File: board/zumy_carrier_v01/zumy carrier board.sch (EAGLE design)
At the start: 22 parts, among them IC1 SN74AUP2G17, IC2 SN74AUP2G17, J1 ODROID_POWER, J2 BATT_POWER, SW1 500SSP1S1M6QEA

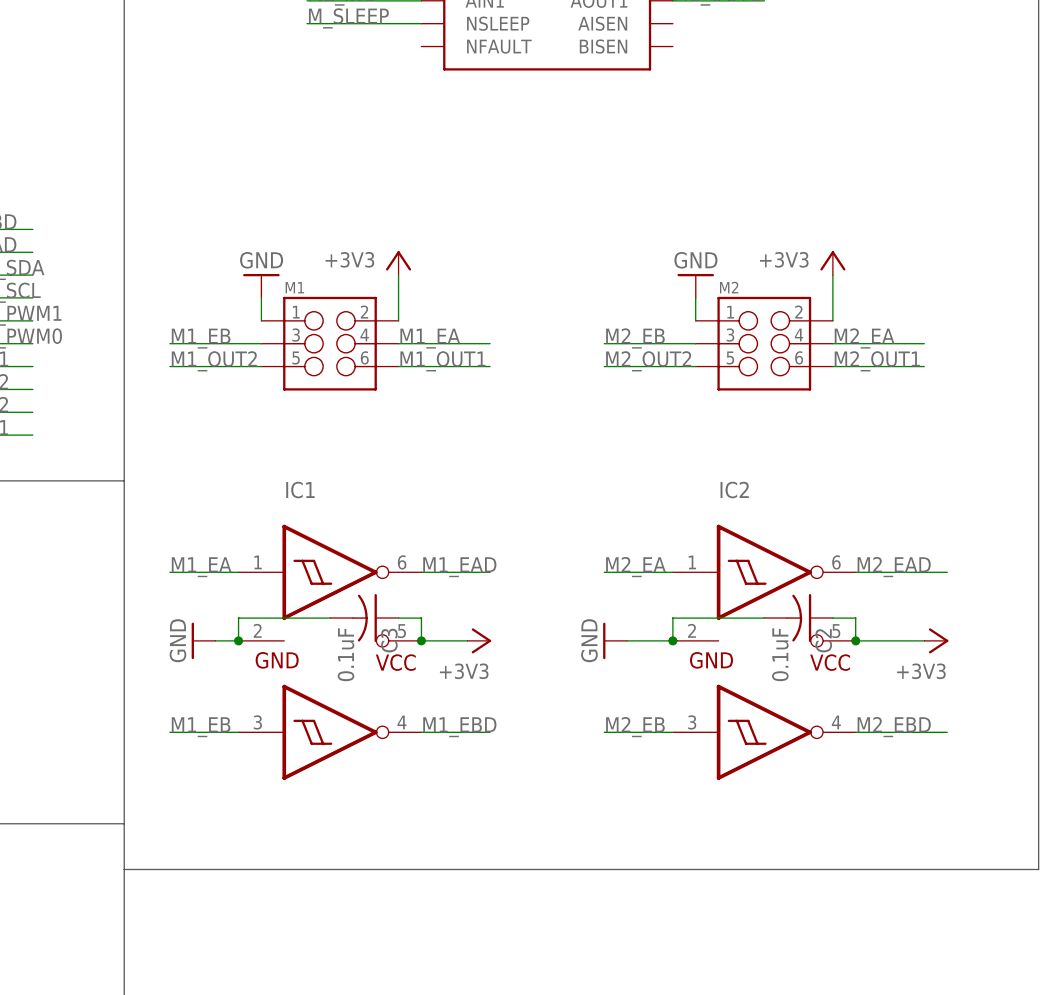
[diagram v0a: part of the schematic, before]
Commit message: Pulled back switch from edge, just need to fix silkscreen.
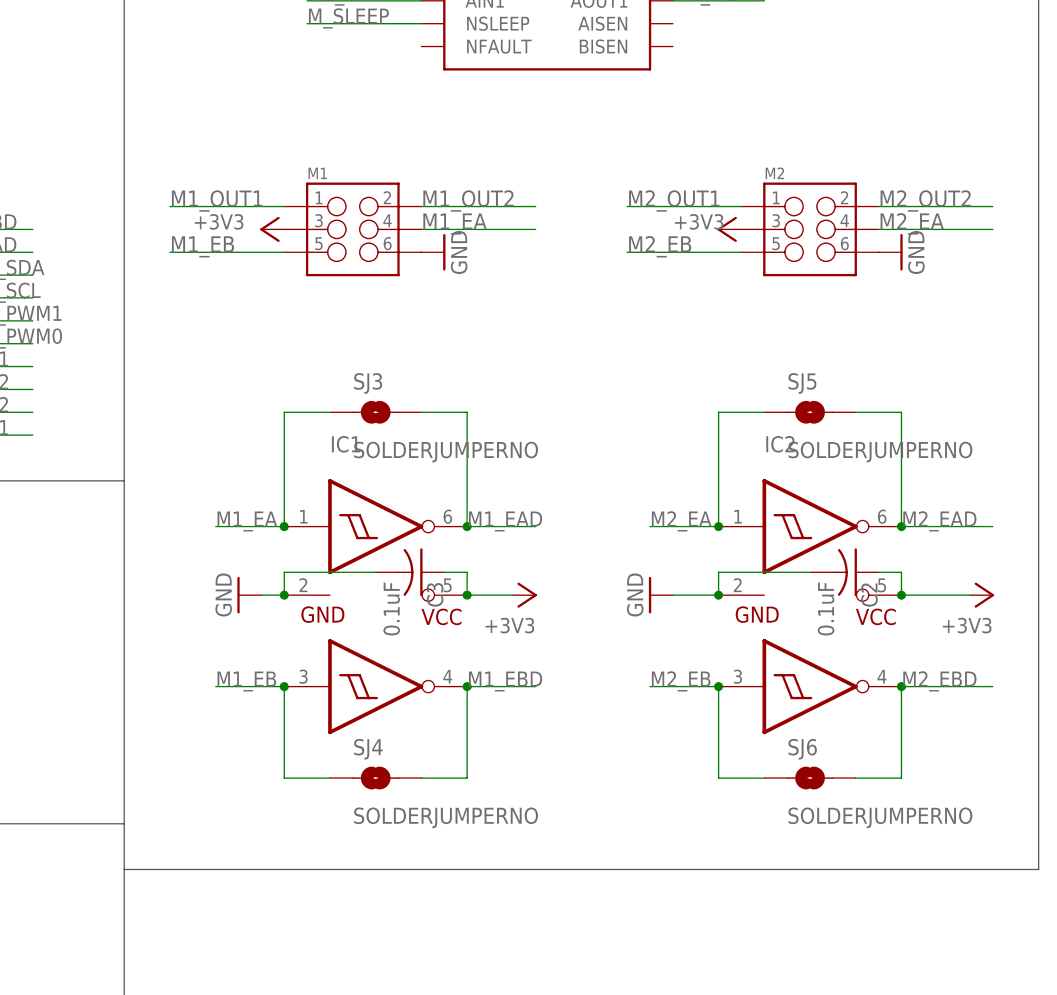
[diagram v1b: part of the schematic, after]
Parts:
- added SJ3, SJ4, SJ5, SJ6: SOLDERJUMPERNO, SparkFun-Passives:SOLDERJUMPERNO
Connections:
- net +3V3: now also M1.3, M2.3; no longer M1.2, M2.2
- net GND: now also M1.6, M2.6; no longer M1.1, M2.1
- net M1_EA: now also SJ3.1
- net M1_EAD: now also SJ3.2
- net M1_EB: now also M1.5, SJ4.1; no longer M1.3
- net M1_EBD: now also SJ4.2
- net M1_OUT1: now also M1.1; no longer M1.6
- net M1_OUT2: now also M1.2; no longer M1.5
- net M2_EA: now also SJ5.1
- net M2_EAD: now also SJ5.2
- net M2_EB: now also M2.5, SJ6.1; no longer M2.3
- net M2_EBD: now also SJ6.2
- net M2_OUT1: now also M2.1; no longer M2.6
- net M2_OUT2: now also M2.2; no longer M2.5
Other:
- moved on the sheet: C2, C3, IC1, IC2, M1, M2
